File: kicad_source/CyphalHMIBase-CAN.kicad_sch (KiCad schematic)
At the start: 27 parts, among them CN1 SM04B-SRSS-TB, CN2 DNI, CN3 SM04B-SRSS-TB, CN4 RASPBERRYPI_PICO, SW1 PTS636 SM43 SMTR LFS, U1 M24C64-RMN6TP

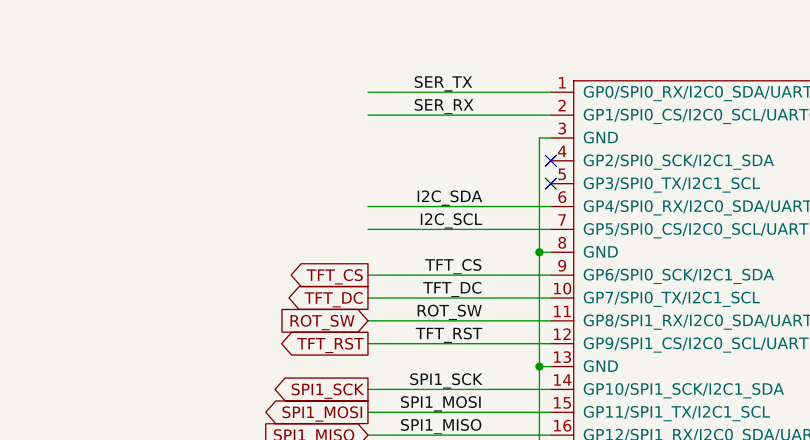
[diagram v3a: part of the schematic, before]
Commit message: added push button
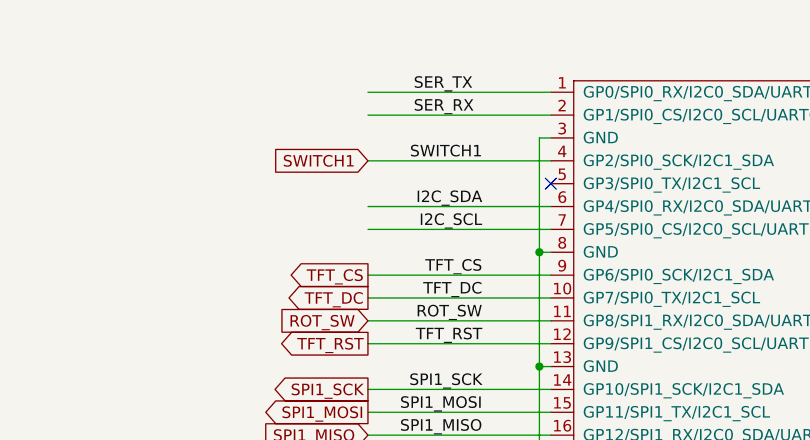
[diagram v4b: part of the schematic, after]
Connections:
- net SWITCH1: now reaches CN4.4 (GP2/SPI0_SCK/I2C1_SDA)
- no-connect marks 9 -> 8
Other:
- title: CyphalIMUBase/CAN -> CyphalHMIBase/CAN
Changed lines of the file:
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@@
 	(paper "A4")
 	(title_block
-		(title "CyphalIMUBase/CAN")
+		(title "CyphalHMIBase/CAN")
 		(date "2026-06-05")
 		(rev "0.1")
@@
 	)
 	(no_connect
-		(at 140.97 31.75)
-	)
-	(no_connect
 		(at 93.98 193.04)
 	)
@@
 		(pts
 			(xy 68.58 132.08) (xy 74.93 132.08)
+		)
+		(stroke
+			(width 0)
+			(type default)
+		)
+	)
+	(wire
+		(pts
+			(xy 120.65 31.75) (xy 140.97 31.75)
 		)
 		(stroke
@@
 			)
 			(justify left bottom)
+		)
+	)
+	(label "SWITCH1"
+		(at 133.35 31.75 180)
+		(effects
+			(font
+				(size 1.27 1.27)
+			)
+			(justify right bottom)
 		)
 	)
@@
 			(effects
 				(font
+					(size 1.27 1.27)
+				)
+				(justify right)
+				(hide yes)
+			)
+		)
+	)
+	(global_label "SWITCH1"
+		(shape input)
+		(at 120.65 31.75 180)
+		(fields_autoplaced yes)
+		(effects
+			(font
+				(size 1.27 1.27)
+			)
+			(justify right)
+		)
+		(property "Intersheetrefs" "${INTERSHEET_REFS}"
+			(at 110.2757 31.75 0)
+			(effects
+				(font
+					(size 1.27 1.27)
+				)
+				(justify right)
+				(hide yes)
+			)
+		)
+		(property "Referenzen zwischen Schaltplänen" "${INTERSHEET_REFS}"
+			(at 120.65 33.5852 0)
+			(effects
+				(font

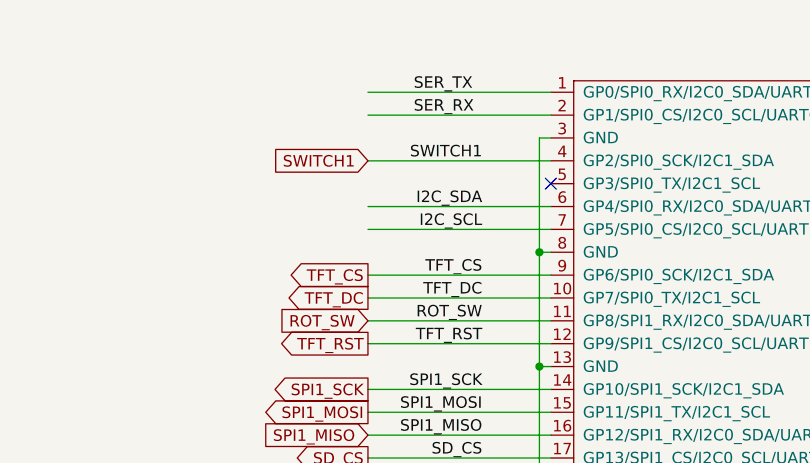
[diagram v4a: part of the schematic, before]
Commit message: added backlight control
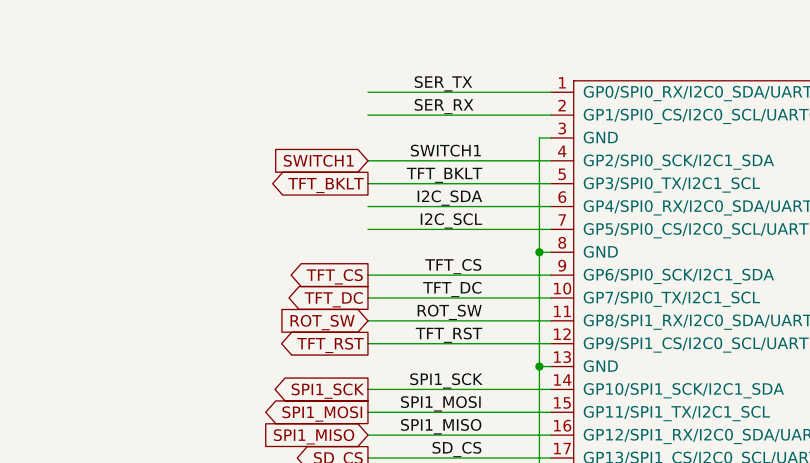
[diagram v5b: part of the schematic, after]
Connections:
- net TFT_BKLT: now reaches CN4.5 (GP3/SPI0_TX/I2C1_SCL)
- no-connect marks 8 -> 7
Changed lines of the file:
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@@
-	)
-	(no_connect
-		(at 140.97 34.29)
 	)
 	(no_connect
@@
 		(pts
 			(xy 120.65 44.45) (xy 140.97 44.45)
+		)
+		(stroke
+			(width 0)
+			(type default)
+		)
+	)
+	(wire
+		(pts
+			(xy 120.65 34.29) (xy 140.97 34.29)
 		)
 		(stroke
@@
 	(label "I2C_SCL"
 		(at 133.35 39.37 180)
+		(effects
+			(font
+				(size 1.27 1.27)
+			)
+			(justify right bottom)
+		)
+	)
+	(label "TFT_BKLT"
+		(at 133.35 34.29 180)
 		(effects
 			(font
@@
 				(hide yes)
 			)
+		)
+	)
+	(global_label "TFT_BKLT"
+		(shape output)
+		(at 120.65 34.29 180)
+		(fields_autoplaced yes)
+		(effects
+			(font
+				(size 1.27 1.27)
+			)
+			(justify right)
+		)
+		(property "Intersheetrefs" "${INTERSHEET_REFS}"
+			(at 109.7919 34.29 0)
+			(effects
+				(font
+					(size 1.27 1.27)
+				)
+				(justify right)
+				(hide yes)
+			)
+		)
+		(property "Referenzen zwischen Schaltplänen" "${INTERSHEET_REFS}"
+			(at 120.65 36.1252 0)
+			(effects
+				(font
+					(size 1.27 1.27)
+				)
+				(justify right)
+				(hide yes)
+			)

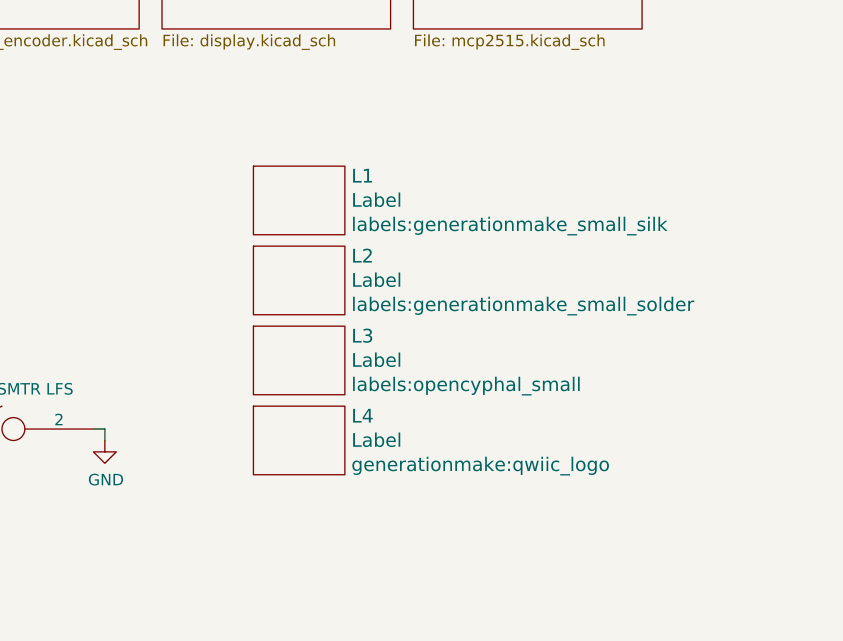
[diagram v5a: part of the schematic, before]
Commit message: fixed drc errors
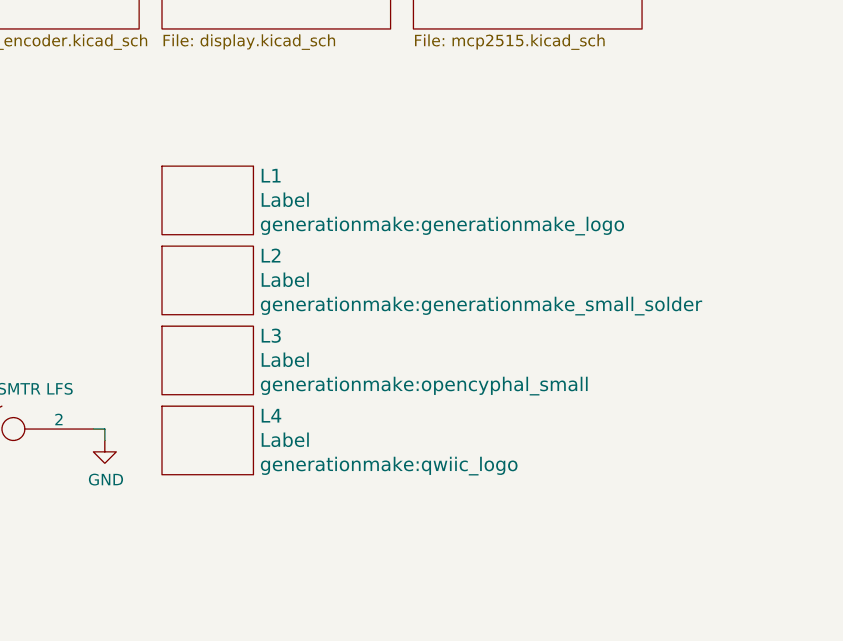
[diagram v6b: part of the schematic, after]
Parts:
- CN4: footprint generationmake:RASPI_PICO_SOLDER_Kopie -> generationmake:RASPI_PICO_SOLDER_ONLY
- L1: footprint labels:generationmake_small_silk -> generationmake:generationmake_logo
- L2: footprint labels:generationmake_small_solder -> generationmake:generationmake_small_solder
- L3: footprint labels:opencyphal_small -> generationmake:opencyphal_small
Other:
- moved on the sheet: L1, L2, L3, L4
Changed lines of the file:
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@@
 	(title_block
 		(title "CyphalHMIBase/CAN")
-		(date "2026-06-05")
+		(date "2026-06-06")
 		(rev "0.1")
 		(company "generationmake")
@@
 	(symbol
 		(lib_id "OpenCyphalPicoBase-rescue:Label-devices")
-		(at 236.22 133.35 0)
+		(at 226.06 133.35 0)
 		(unit 1)
 		(exclude_from_sim no)
@@
 		(dnp no)
 		(property "Reference" "L1"
-			(at 242.0112 130.6576 0)
+			(at 231.8512 130.6576 0)
 			(effects
 				(font
@@
 		)
 		(property "Value" "Label"
-			(at 242.0112 133.35 0)
+			(at 231.8512 133.35 0)
 			(effects
 				(font
@@
 			)
 		)
-		(property "Footprint" "labels:generationmake_small_silk"
-			(at 242.0112 136.0424 0)
+		(property "Footprint" "generationmake:generationmake_logo"
+			(at 231.8512 136.0424 0)
 			(effects
 				(font
@@
 		)
 		(property "Datasheet" ""
-			(at 236.22 133.35 0)
+			(at 226.06 133.35 0)
 			(effects
 				(font
@@
 		)
 		(property "Description" ""
-			(at 236.22 133.35 0)
+			(at 226.06 133.35 0)
 			(effects
 				(font
@@
 	(symbol
 		(lib_id "OpenCyphalPicoBase-rescue:Label-devices")
-		(at 236.22 142.24 0)
+		(at 226.06 142.24 0)
 		(unit 1)
 		(exclude_from_sim no)
@@
 		(dnp no)
 		(property "Reference" "L2"
-			(at 242.0112 139.5476 0)
+			(at 231.8512 139.5476 0)
 			(effects
 				(font
@@
 		)
 		(property "Value" "Label"
-			(at 242.0112 142.24 0)
+			(at 231.8512 142.24 0)
 			(effects
 				(font
@@
 			)
 		)
-		(property "Footprint" "labels:generationmake_small_solder"
-			(at 242.0112 144.9324 0)
+		(property "Footprint" "generationmake:generationmake_small_solder"
+			(at 231.8512 144.9324 0)
 			(effects
 				(font
@@
 		)
 		(property "Datasheet" ""
-			(at 236.22 142.24 0)
+			(at 226.06 142.24 0)
 			(effects
 				(font
@@
 		)
 		(property "Description" ""
-			(at 236.22 142.24 0)
+			(at 226.06 142.24 0)
 			(effects
 				(font
@@
 	(symbol
 		(lib_id "OpenCyphalPicoBase-rescue:Label-devices")
-		(at 236.22 151.13 0)
+		(at 226.06 151.13 0)
 		(unit 1)
 		(exclude_from_sim no)
@@
 		(dnp no)
 		(property "Reference" "L3"
-			(at 242.0112 148.4376 0)
+			(at 231.8512 148.4376 0)
 			(effects
 				(font
@@
 		)
 		(property "Value" "Label"
-			(at 242.0112 151.13 0)
+			(at 231.8512 151.13 0)
 			(effects
 				(font
@@
 			)
 		)
-		(property "Footprint" "labels:opencyphal_small"
-			(at 242.0112 153.8224 0)
+		(property "Footprint" "generationmake:opencyphal_small"
+			(at 231.8512 153.8224 0)
 			(effects
 				(font
@@
 		)
 		(property "Datasheet" ""
-			(at 236.22 151.13 0)
+			(at 226.06 151.13 0)
 			(effects
 				(font
@@
 		)
 		(property "Description" ""
-			(at 236.22 151.13 0)
+			(at 226.06 151.13 0)
 			(effects
 				(font
@@
 			)
 		)
-		(property "Footprint" "generationmake:RASPI_PICO_SOLDER_Kopie"
+		(property "Footprint" "generationmake:RASPI_PICO_SOLDER_ONLY"
 			(at 180.34 48.26 0)
 			(effects
@@
 	(symbol
 		(lib_id "OpenCyphalPicoBase-rescue:Label-devices")
-		(at 236.22 160.02 0)
+		(at 226.06 160.02 0)
 		(unit 1)
 		(exclude_from_sim no)
@@
 		(dnp no)
 		(property "Reference" "L4"
-			(at 242.0112 157.3276 0)
+			(at 231.8512 157.3276 0)
 			(effects
 				(font
@@
 		)
 		(property "Value" "Label"
-			(at 242.0112 160.02 0)
+			(at 231.8512 160.02 0)
 			(effects
 				(font
@@
 		)
 		(property "Footprint" "generationmake:qwiic_logo"
-			(at 242.0112 162.7124 0)
+			(at 231.8512 162.7124 0)
 			(effects
 				(font
@@
 		)
 		(property "Datasheet" ""
-			(at 236.22 160.02 0)
+			(at 226.06 160.02 0)
 			(effects
 				(font
@@
 		)
 		(property "Description" ""
-			(at 236.22 160.02 0)
+			(at 226.06 160.02 0)
 			(effects
 				(font
